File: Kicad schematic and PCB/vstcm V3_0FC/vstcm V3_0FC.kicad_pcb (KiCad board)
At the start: 2 copper layers, 100 x 100 mm, 101 parts, among them IC1 TL3474, IC2 RB-0512D, IC3 MCP4922-E/P, IC4 MCP4922-E/P, IC5 MCP4922-E/P, IC6 TL3474, J1 Conn_01x24_Male, J2 Conn_01x05_Male, J3 Conn_01x25_Male, J6 Conn_01x02_Male, J7 Conn_01x03_Male, J8 Conn_01x01_Male, J9 Conn_01x02_Male, SW1 SW_Push, SW2 SW_Push, SW3 SW_Push, SW4 SW_Push, SW5 SW_Push, U1 Teensy4.1, U3 LP2950-3_3_TO92, U5 LM2940T-5.0

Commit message: Animated vector fonts is a demo
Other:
- board text added: "VSTCM v.st colour mod v3.0"
- board text removed: "v.st colour mod v3.0"

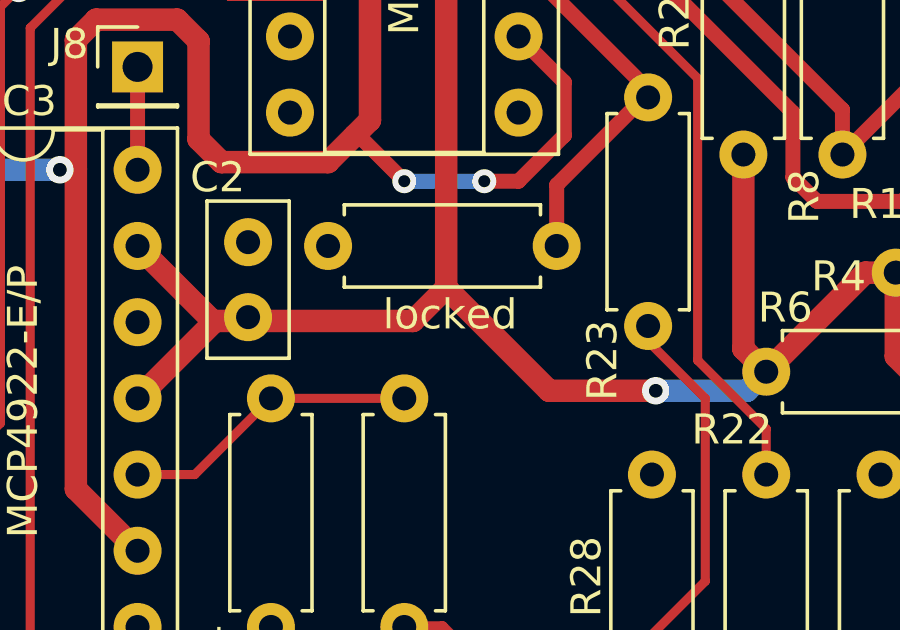
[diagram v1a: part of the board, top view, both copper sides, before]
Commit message: More info on type of IC sockets and mounting for Teensy; Kicad files updated to v8.
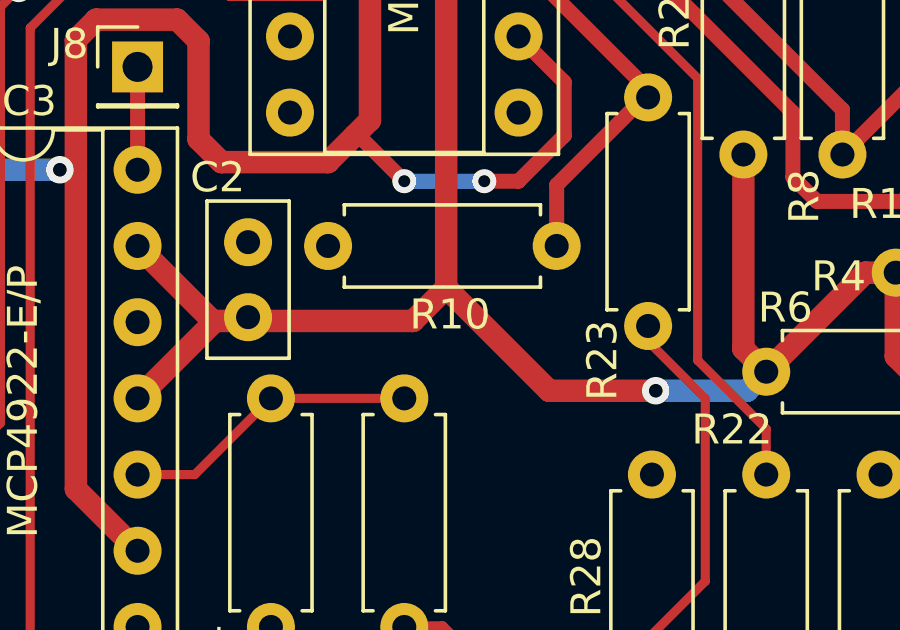
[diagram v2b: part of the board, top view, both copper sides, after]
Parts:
- renumbered locked to R10
